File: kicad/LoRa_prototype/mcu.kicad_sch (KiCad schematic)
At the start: 56 parts, among them J14 SPI_FLASH, SW1 NRST, U1 STM32WL55JCIx, U8 W25Q16JVSS, X1 32768Hz, X2 NT2016SF

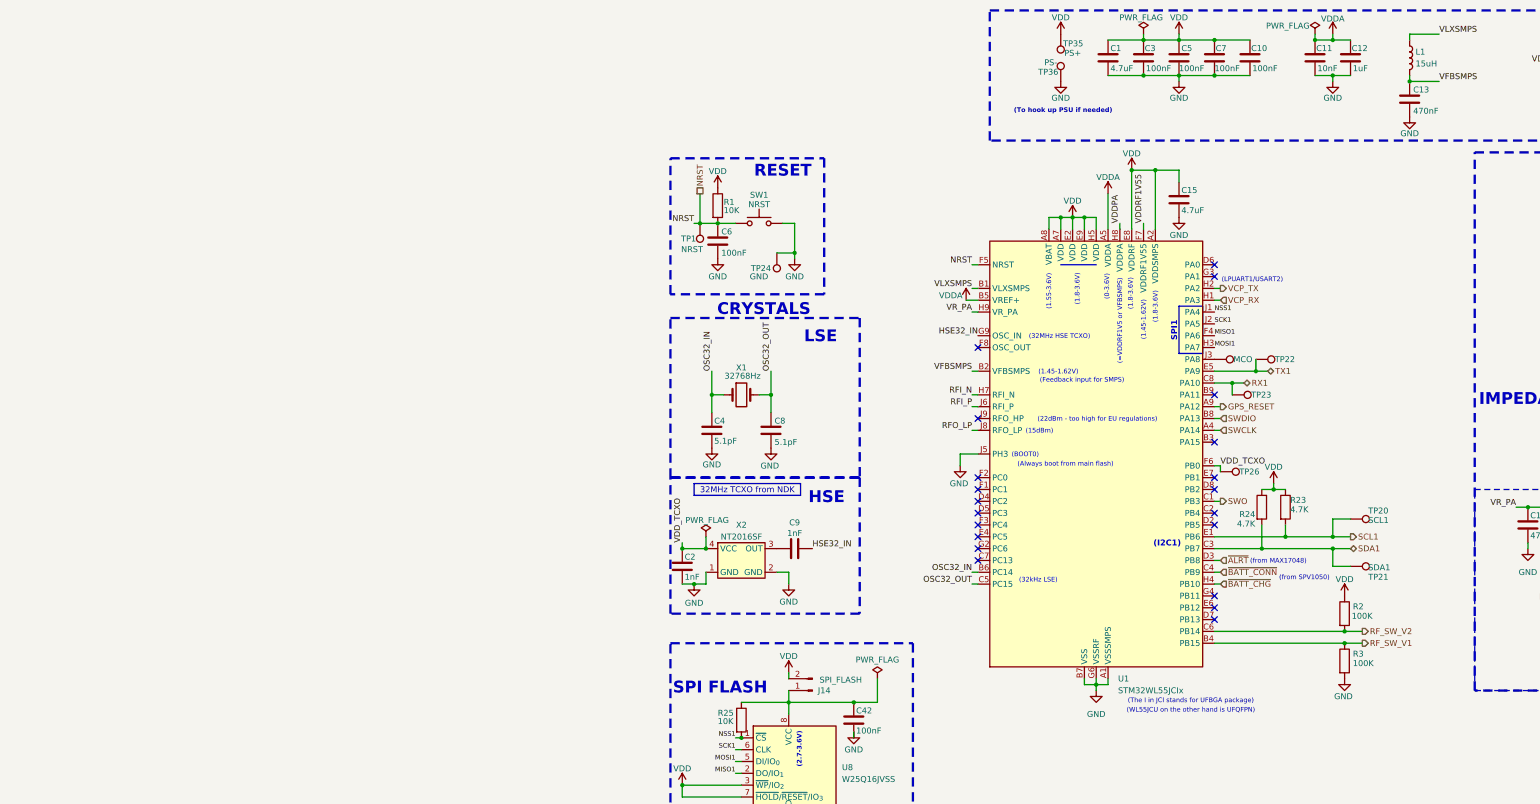
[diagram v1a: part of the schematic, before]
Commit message: Redone schematic with stm32wl55ccu6
The original MCU STM32WL55JCI6 is still left on the schematic so come back here if something is messed up
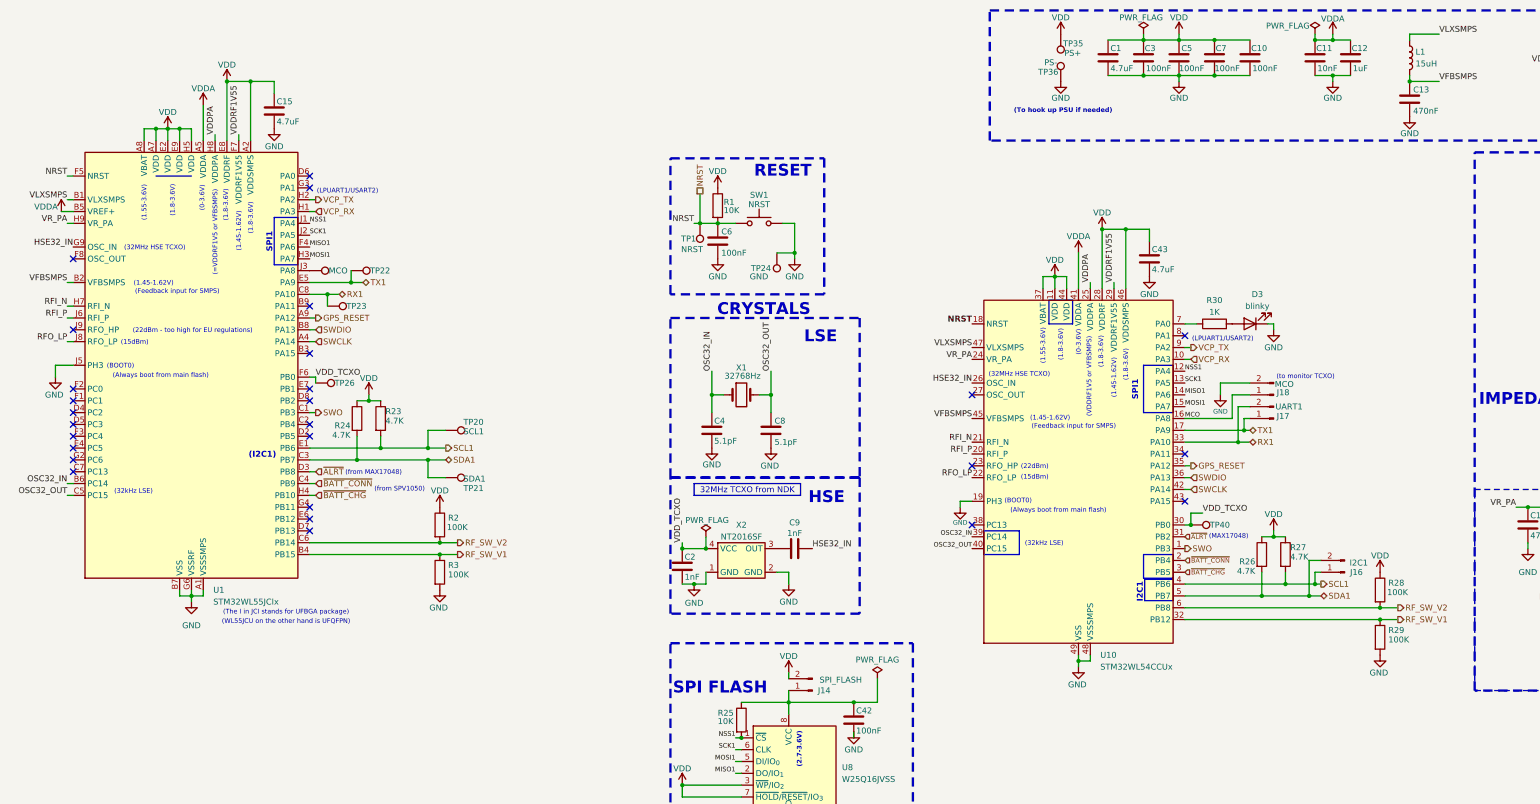
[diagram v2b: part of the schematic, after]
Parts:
- added C43: 4.7uF, Capacitor_SMD:C_0805_2012Metric, symbol Device:C
- added D3: blinky, LED_SMD:LED_0805_2012Metric, symbol Device:LED
- added J16: I2C1, Connector_PinHeader_2.54mm:PinHeader_1x02_P2.54mm_Vertical, symbol Connector:Conn_01x02_Pin
- added J17: UART1, Connector_PinHeader_2.54mm:PinHeader_1x02_P2.54mm_Vertical, symbol Connector:Conn_01x02_Pin
- added J18: MCO, Connector_PinHeader_2.54mm:PinHeader_1x02_P2.54mm_Vertical, symbol Connector:Conn_01x02_Pin
- added R26, R27: 4.7K, Resistor_SMD:R_0805_2012Metric, symbol Device:R
- added R28, R29: 100K, Resistor_SMD:R_0805_2012Metric, symbol Device:R
- added R30: 1K, Resistor_SMD:R_0805_2012Metric, symbol Device:R
- added TP40: VDDXO, TestPoint:TestPoint_Pad_2.0x2.0mm, symbol Connector:TestPoint
- added U10: STM32WL54CCUx, Package_DFN_QFN:QFN-48-1EP_7x7mm_P0.5mm_EP5.6x5.6mm, symbol MCU_ST_STM32WL:STM32WL54CCUx
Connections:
- net GND: now also C43.2, D3.1 (K), J18.2 (Pin_2), R29.2, U10.19 (PH3), U10.48 (VSSSMPS), U10.49 (VSS)
- net GPS_RESET: now also U10.35 (PA12)
- net HSE32_IN: now also U10.26 (OSC_IN)
- net MISO1: now also U10.14 (PA6)
- net MOSI1: now also U10.15 (PA7)
- net NRST: now also U10.18 (NRST)
- net NSS1: now also U10.12 (PA4)
- net OSC32_IN: now also U10.39 (PC14)
- net OSC32_OUT: now also U10.40 (PC15)
- net RFI_N: now also U10.21 (RFI_N)
- net RFI_P: now also U10.20 (RFI_P)
- net RFO_LP: now also U10.22 (RFO_LP)
- net RF_SW_V1: now also R29.1, U10.32 (PB12)
- net RF_SW_V2: now also R28.2, U10.6 (PB8)
- net RX1: now also J17.2 (Pin_2), U10.33 (PA10)
- net SCK1: now also U10.13 (PA5)
- net SCL1: now also J16.1 (Pin_1), R27.2, U10.4 (PB6)
- net SDA1: now also J16.2 (Pin_2), R26.2, U10.5 (PB7)
- net SWCLK: now also U10.42 (PA14)
- net SWDIO: now also U10.36 (PA13)
- net SWO: now also U10.1 (PB3)
- net TX1: now also J17.1 (Pin_1), U10.17 (PA9)
- net VCP_RX: now also U10.10 (PA3)
- net VCP_TX: now also U10.9 (PA2)
- net VDD: now also C43.1, R26.1, R27.1, R28.1, U10.11 (VDD), U10.28 (VDDRF), U10.37 (VBAT), U10.44 (VDD), U10.46 (VDDSMPS)
- net VDDA: now also U10.41 (VDDA)
- net VDDPA: now also U10.25 (VDDPA)
- net VDDRF1V55: now also U10.29 (VDDRF1V55)
- net VDD_TCXO: now also TP40.1, U10.30 (PB0)
- net VFBSMPS: now also U10.45 (VFBSMPS)
- net VLXSMPS: now also U10.47 (VLXSMPS)
- net VR_PA: now also U10.24 (VR_PA)
- net ~{ALRT}: now also U10.31 (PB2)
- net ~{BATT_CHG}: now also U10.3 (PB5)
- net ~{BATT_CONN}: now also U10.2 (PB4)
- new net: R30.1, U10.7 (PA0)
- new net: D3.2 (A), R30.2
- new net MCO: J18.1 (Pin_1), U10.16 (PA8)
- no-connect marks 21 -> 27
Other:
- note added: "(22dBm)"
- note added: "(MAX17048)"
- note added: "(VDDRF1V5 or VFBSMPS)"
- note added: "(to monitor TCXO)"
- note added: "I2C1"
- moved on the sheet: C15, R2, R23, R24, R3, TP20, TP21, TP22, TP23, TP26, U1

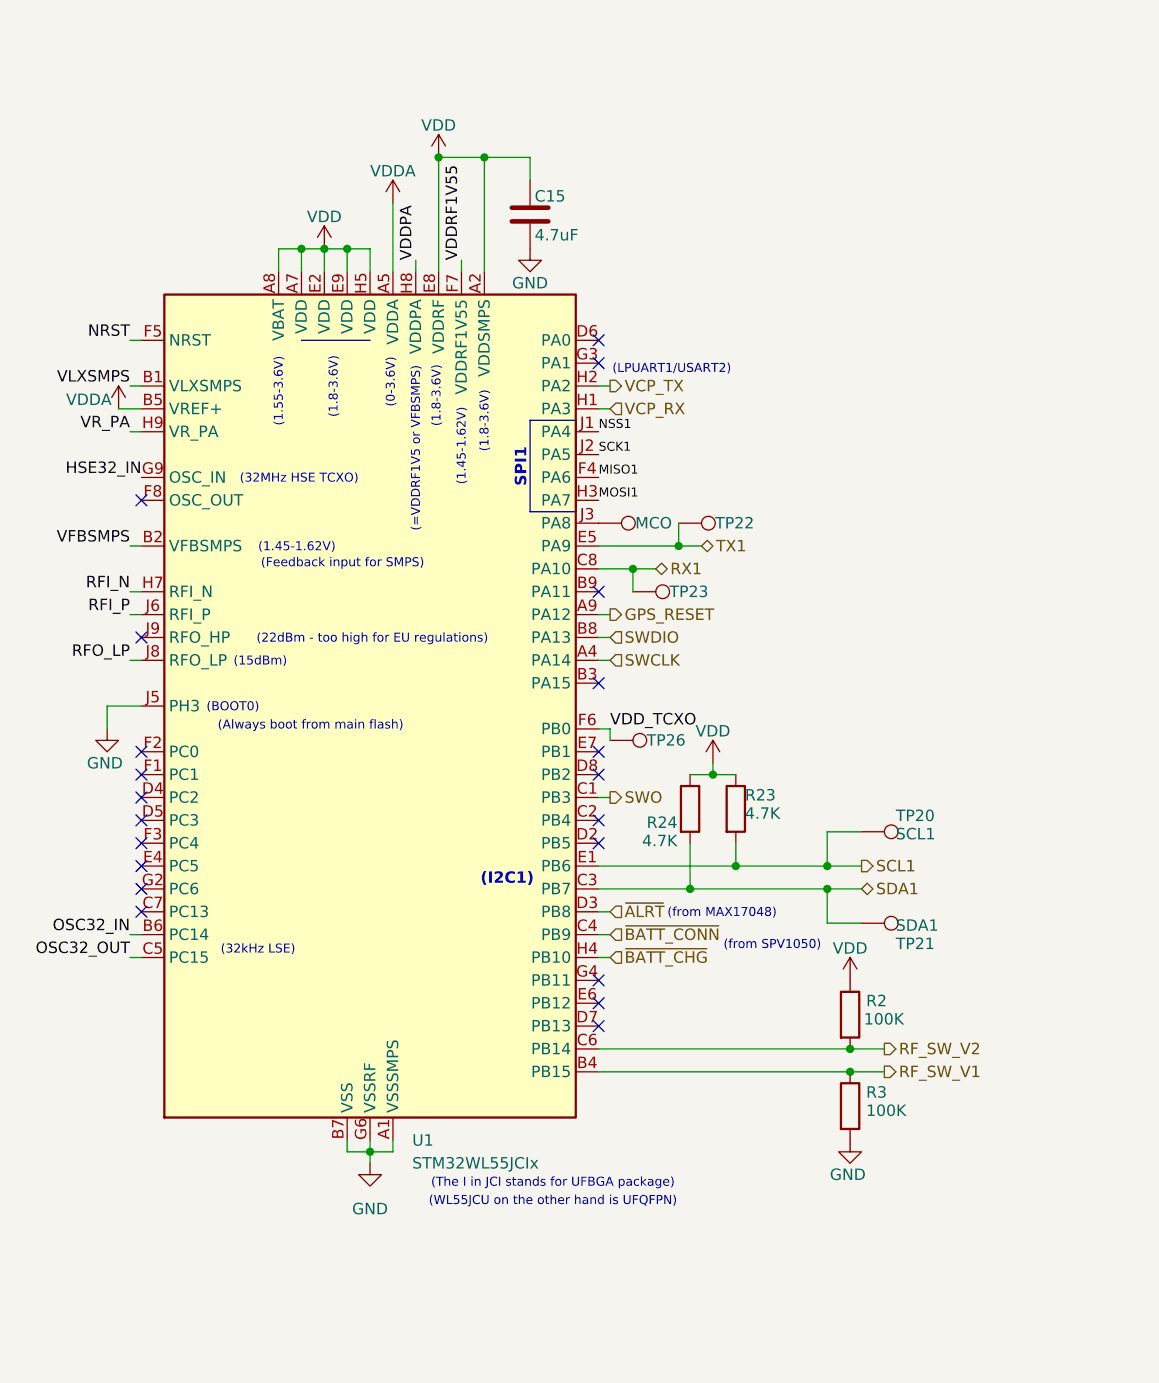
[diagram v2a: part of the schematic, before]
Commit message: Finally removed stm32wl55jci6
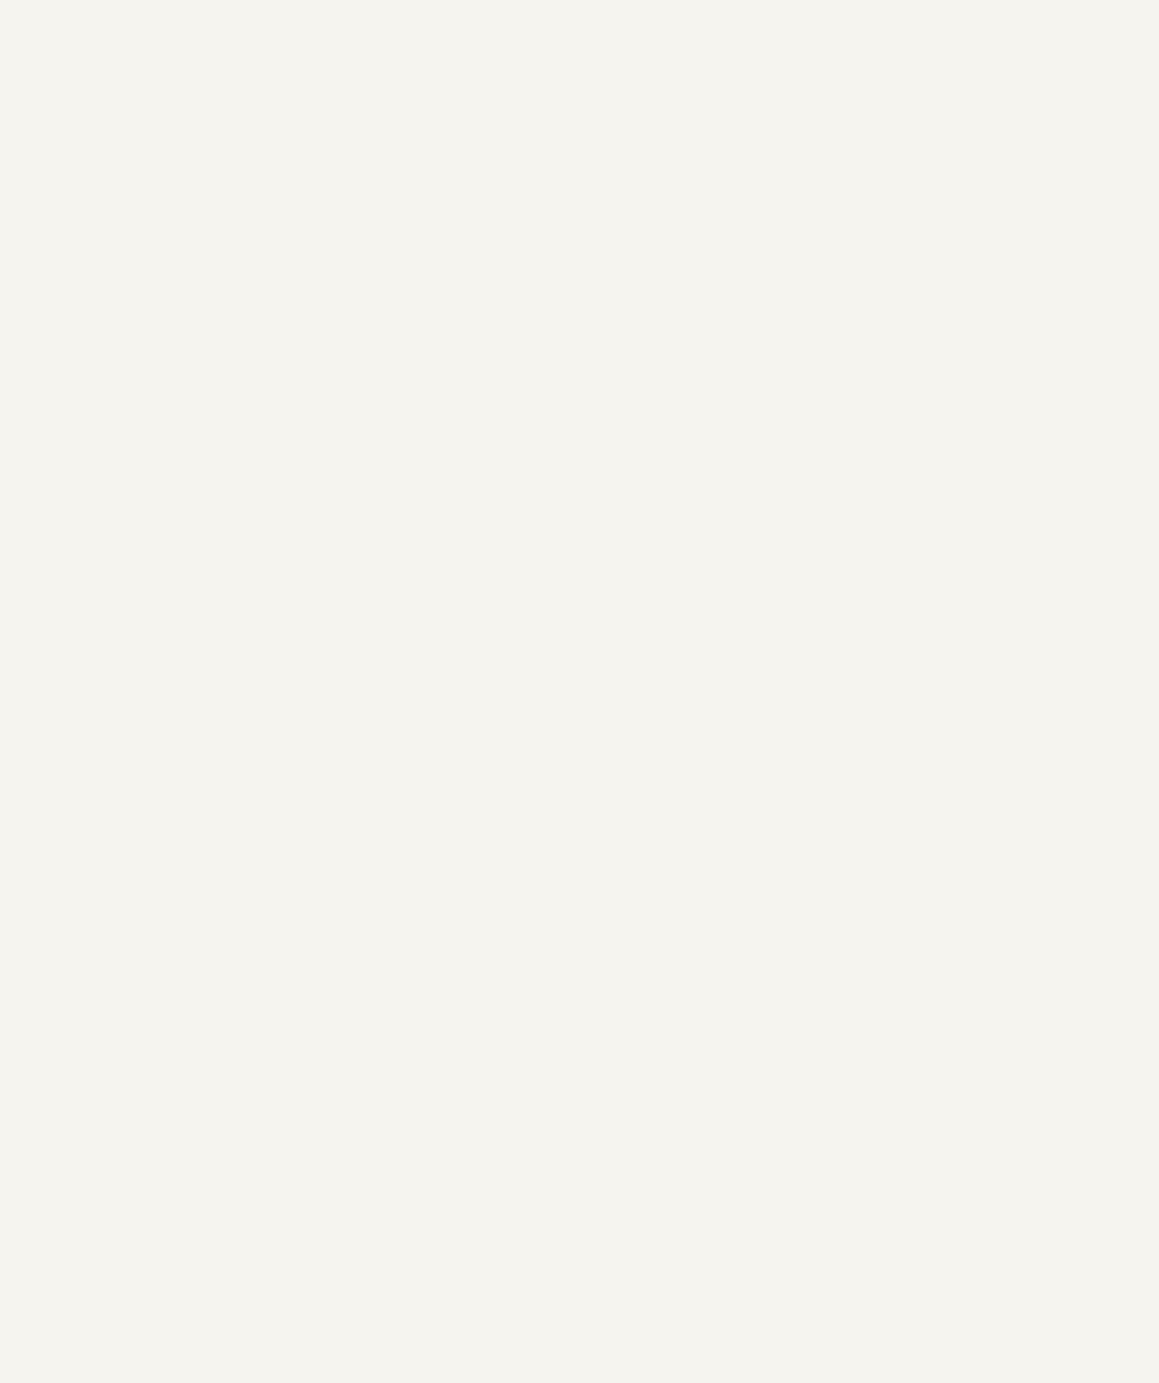
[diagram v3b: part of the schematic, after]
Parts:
- removed C15: 4.7uF, Capacitor_SMD:C_0805_2012Metric, symbol Device:C
- removed R2, R3: 100K, Resistor_SMD:R_0805_2012Metric, symbol Device:R
- removed R23, R24: 4.7K, Resistor_SMD:R_0805_2012Metric, symbol Device:R
- removed TP20: SCL1, Connector_PinHeader_2.54mm:PinHeader_1x01_P2.54mm_Vertical, symbol Connector:TestPoint
- removed TP21: SDA1, Connector_PinHeader_2.54mm:PinHeader_1x01_P2.54mm_Vertical, symbol Connector:TestPoint
- removed TP22: TX1, Connector_PinHeader_2.54mm:PinHeader_1x01_P2.54mm_Vertical, symbol Connector:TestPoint
- removed TP23: RX1, Connector_PinHeader_2.54mm:PinHeader_1x01_P2.54mm_Vertical, symbol Connector:TestPoint
- removed TP25: MCO, Connector_PinHeader_2.54mm:PinHeader_1x01_P2.54mm_Vertical, symbol Connector:TestPoint
- removed TP26: VDDXO, TestPoint:TestPoint_Pad_2.0x2.0mm, symbol Connector:TestPoint
- removed U1: STM32WL55JCIx, Package_BGA:ST_UFBGA-73_5x5mm_Layout9x9_P0.5mm, symbol MCU_ST_STM32WL:STM32WL55JCIx
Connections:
- no-connect marks 27 -> 6
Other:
- note removed: "(22dBm - too high for EU regulations)"
- note removed: "(=VDDRF1V5 or VFBSMPS)"
- note removed: "(I2C1)"
- note removed: "(The I in JCI stands for UFBGA package)"
- note removed: "(WL55JCU on the other hand is UFQFPN)"
- note removed: "(from MAX17048)"
- note removed: "(from SPV1050)"

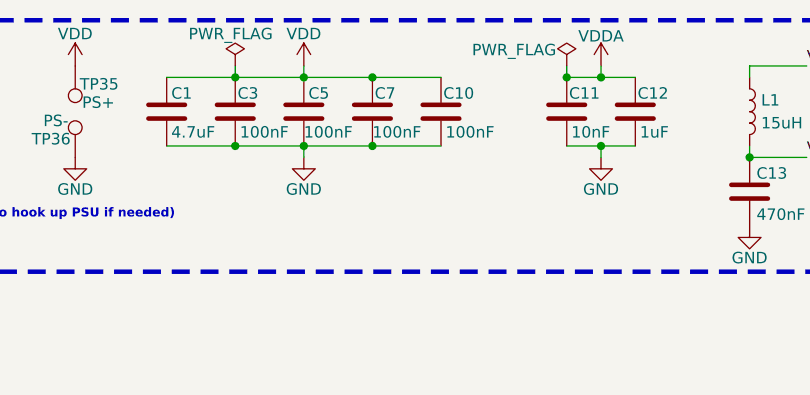
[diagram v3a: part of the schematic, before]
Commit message: Removed redundant I2C test pin headers
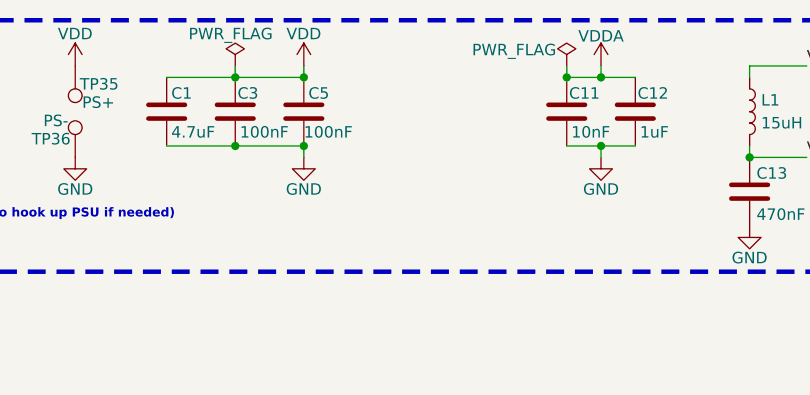
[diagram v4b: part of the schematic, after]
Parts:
- removed C10, C7: 100nF, Capacitor_SMD:C_0805_2012Metric, symbol Device:C

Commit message: Updated component values to match E24 series
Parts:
- C20: value 7.7pF -> 8.2pF
- C21: value 3.3pF -> 3pF
- C22: value 3.6pF -> 0.75pF
- C24: value 3pF -> 4.7pF
- C25: value 1.4pF -> 3pF
- C26: value 2.2pF -> 3pF
- L2: value 3.5nH -> 3.6nH
- L4: value 2.6nH -> 2.7nH
- L5: value 7.5nH -> 10nH
- L6: value 12nH -> 10nH
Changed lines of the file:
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@@
 		)
 	)
+	(text_box "RF components:\n\nHigh-Q Murata GJM15 series for caps\nHigh-Q Murata LQW15AN series for inductors\n\n"
+		(exclude_from_sim no)
+		(at 93.98 169.418 0)
+		(size 46.736 10.4163)
+		(margins 0.9525 0.9525 0.9525 0.9525)
+		(stroke
+			(width 0.25)
+			(type solid)
+		)
+		(fill
+			(type color)
+			(color 255 249 106 1)
+		)
+		(effects
+			(font
+				(size 1.27 1.27)
+				(thickness 0.254)
+				(bold yes)
+			)
+			(justify left top)
+		)
+	)
 	(junction
 		(at 20.32 58.42)
@@
 			)
 		)
-		(property "Value" "12nH"
+		(property "Value" "10nH"
 			(at 248.92 95.2499 0)
 			(show_name no)
@@
 			)
 		)
-		(property "Value" "3.3pF"
+		(property "Value" "3pF"
 			(at 222.25 130.048 90)
 			(show_name no)
@@
 			)
 		)
-		(property "Value" "3.6pF"
+		(property "Value" "0.75pF"
 			(at 226.314 148.59 0)
 			(show_name no)
@@
 			)
 		)
-		(property "Value" "1.4pF"
+		(property "Value" "3pF"
 			(at 250.444 148.59 0)
 			(show_name no)
@@
 			)
 		)
-		(property "Value" "3pF"
+		(property "Value" "4.7pF"
 			(at 248.158 103.886 0)
 			(show_name no)
@@
 			)
 		)
-		(property "Value" "2.2pF"
+		(property "Value" "3pF"
 			(at 254 86.868 90)
 			(show_name no)
@@
 			)
 		)
-		(property "Value" "7.5nH"
+		(property "Value" "10nH"
 			(at 242.57 137.16 90)
 			(show_name no)
@@
 			)
 		)
-		(property "Value" "3.5nH"
+		(property "Value" "3.6nH"
 			(at 212.09 137.16 90)
 			(show_name no)
@@
 			)
 		)
-		(property "Value" "7.7pF"
+		(property "Value" "8.2pF"
 			(at 218.694 148.59 0)
 			(show_name no)
@@
 			)
 		)
-		(property "Value" "2.6nH"
+		(property "Value" "2.7nH"
 			(at 222.25 137.922 90)
 			(show_name no)
